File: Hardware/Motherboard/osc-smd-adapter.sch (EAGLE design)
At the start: 2 parts

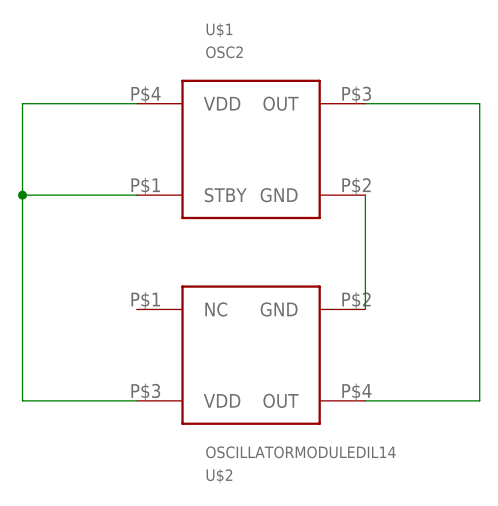
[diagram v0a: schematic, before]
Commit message: Fix flipped SMD oscillator
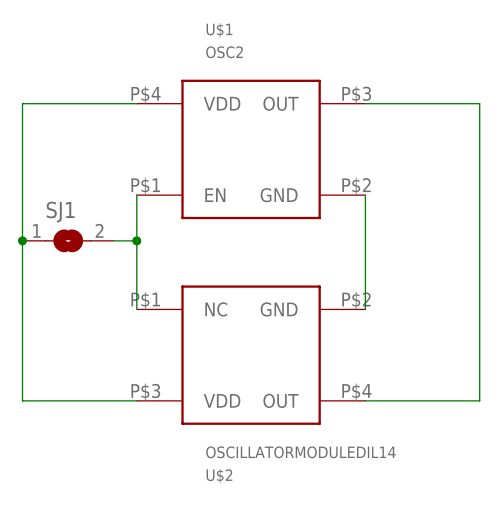
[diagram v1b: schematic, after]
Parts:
- added SJ1: (no value), jumper:SJ
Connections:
- new net N$4: SJ1.2, U$1.EN, U$2.NC
- net N$1: now also SJ1.1; no longer U$1.STBY
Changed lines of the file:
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@@
 <part name="U$1" library="0_gametankparts" deviceset="OSC2" device=""/>
 <part name="U$2" library="0_gametankparts" deviceset="OSCILLATORMODULE" device="DIL14"/>
+<part name="SJ1" library="jumper" library_urn="urn:adsk.eagle:library:252" deviceset="SJ" device="" package3d_urn="urn:adsk.eagle:package:15471/1"/>
 </parts>
 <sheets>
@@
 <attribute name="VALUE" x="81.28" y="48.26" size="1.27" layer="96" rot="MR180"/>
 </instance>
+<instance part="SJ1" gate="1" x="66.04" y="71.12" smashed="yes">
+<attribute name="NAME" x="63.5" y="73.66" size="1.778" layer="95"/>
+<attribute name="VALUE" x="63.5" y="67.31" size="1.778" layer="96"/>
+</instance>
 </instances>
 <busses>
 </busses>
 <nets>
-<net name="N$1" class="0">
-<segment>
-<pinref part="U$1" gate="G$1" pin="VDD"/>
-<wire x1="73.66" y1="86.36" x2="60.96" y2="86.36" width="0.1524" layer="91"/>
-<wire x1="60.96" y1="86.36" x2="60.96" y2="76.2" width="0.1524" layer="91"/>
-<pinref part="U$2" gate="G$1" pin="VDD"/>
-<wire x1="60.96" y1="76.2" x2="60.96" y2="53.34" width="0.1524" layer="91"/>
-<wire x1="60.96" y1="53.34" x2="73.66" y2="53.34" width="0.1524" layer="91"/>
-<pinref part="U$1" gate="G$1" pin="STBY"/>
-<wire x1="73.66" y1="76.2" x2="60.96" y2="76.2" width="0.1524" layer="91"/>
-<junction x="60.96" y="76.2"/>
-</segment>
-</net>
 <net name="N$2" class="0">
 <segment>
@@
 </segment>
 </net>
+<net name="N$1" class="0">
+<segment>
+<pinref part="U$1" gate="G$1" pin="VDD"/>
+<wire x1="73.66" y1="86.36" x2="60.96" y2="86.36" width="0.1524" layer="91"/>
+<pinref part="U$2" gate="G$1" pin="VDD"/>
+<wire x1="60.96" y1="86.36" x2="60.96" y2="71.12" width="0.1524" layer="91"/>
+<wire x1="60.96" y1="71.12" x2="60.96" y2="53.34" width="0.1524" layer="91"/>
+<wire x1="60.96" y1="53.34" x2="73.66" y2="53.34" width="0.1524" layer="91"/>
+<pinref part="SJ1" gate="1" pin="1"/>
+<junction x="60.96" y="71.12"/>
+</segment>
+</net>
+<net name="N$4" class="0">
+<segment>
+<pinref part="U$2" gate="G$1" pin="NC"/>
+<pinref part="U$1" gate="G$1" pin="EN"/>
+<wire x1="73.66" y1="76.2" x2="73.66" y2="71.12" width="0.1524" layer="91"/>
+<pinref part="SJ1" gate="1" pin="2"/>
+<wire x1="73.66" y1="71.12" x2="73.66" y2="63.5" width="0.1524" layer="91"/>
+<wire x1="71.12" y1="71.12" x2="73.66" y2="71.12" width="0.1524" layer="91"/>
+<junction x="73.66" y="71.12"/>
+</segment>
+</net>
 </nets>
 </sheet>
@@
 </schematic>
 </drawing>
+<compatibility>
+<note version="8.2" severity="warning">
+Since Version 8.2, EAGLE supports online libraries. The ids
+of those online libraries will not be understood (or retained)
+with this version.
+</note>
+<note version="8.3" severity="warning">
+Since Version 8.3, EAGLE supports URNs for individual library
+assets (packages, symbols, and devices). The URNs of those assets
+will not be understood (or retained) with this version.
+</note>
+<note version="8.3" severity="warning">
+Since Version 8.3, EAGLE supports the association of 3D packages
+with devices in libraries, schematics, and board files. Those 3D
+packages will not be understood (or retained) with this version.
+</note>
+</compatibility>
 </eagle>
